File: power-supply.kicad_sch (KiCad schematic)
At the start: 107 parts, among them IC1 TPS54561QDPR, J10 Molex_Pico-Lock_1x02_504050-0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, J5 Molex_Pico-Lock_1x02_504050-0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, Q1 BSS138PW, Q2 BSS138PW, Q3 BSS138PW, Q4 BSS138PW, Q5 BSS138PW, Q6 BSS138PW, U10 TPS62823DLCT, U11 TPS62823DLCT, U12 TPS62823DLCT, U13 TPS62823DLCT, U16 TPS62823DLCT, U9 LM3881MME_NOPB

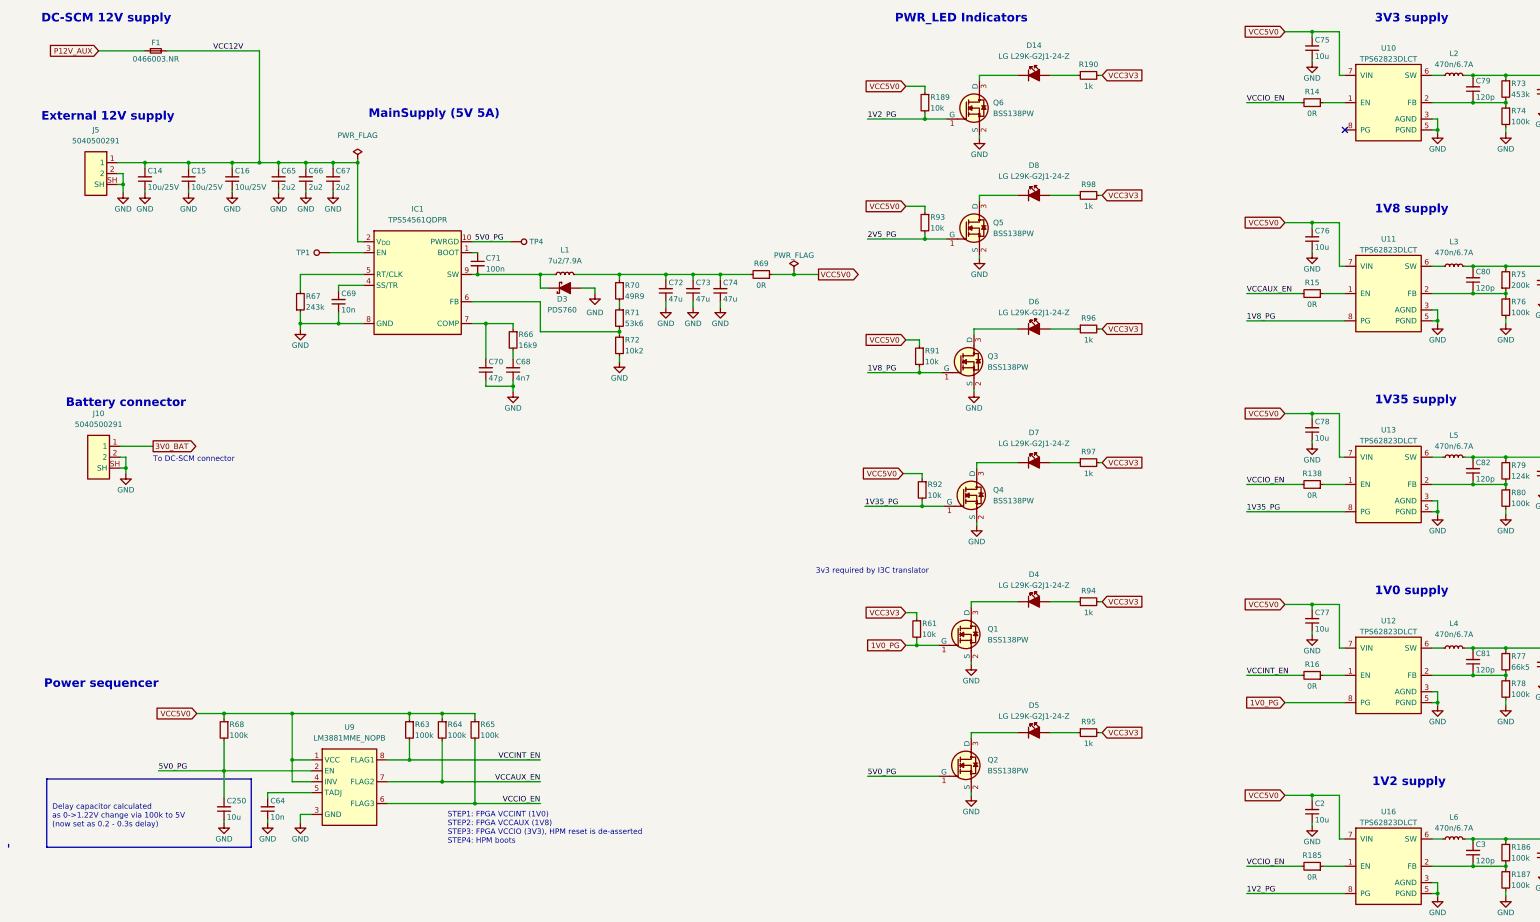
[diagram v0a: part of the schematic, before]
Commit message: [#55652] Fix hotareas
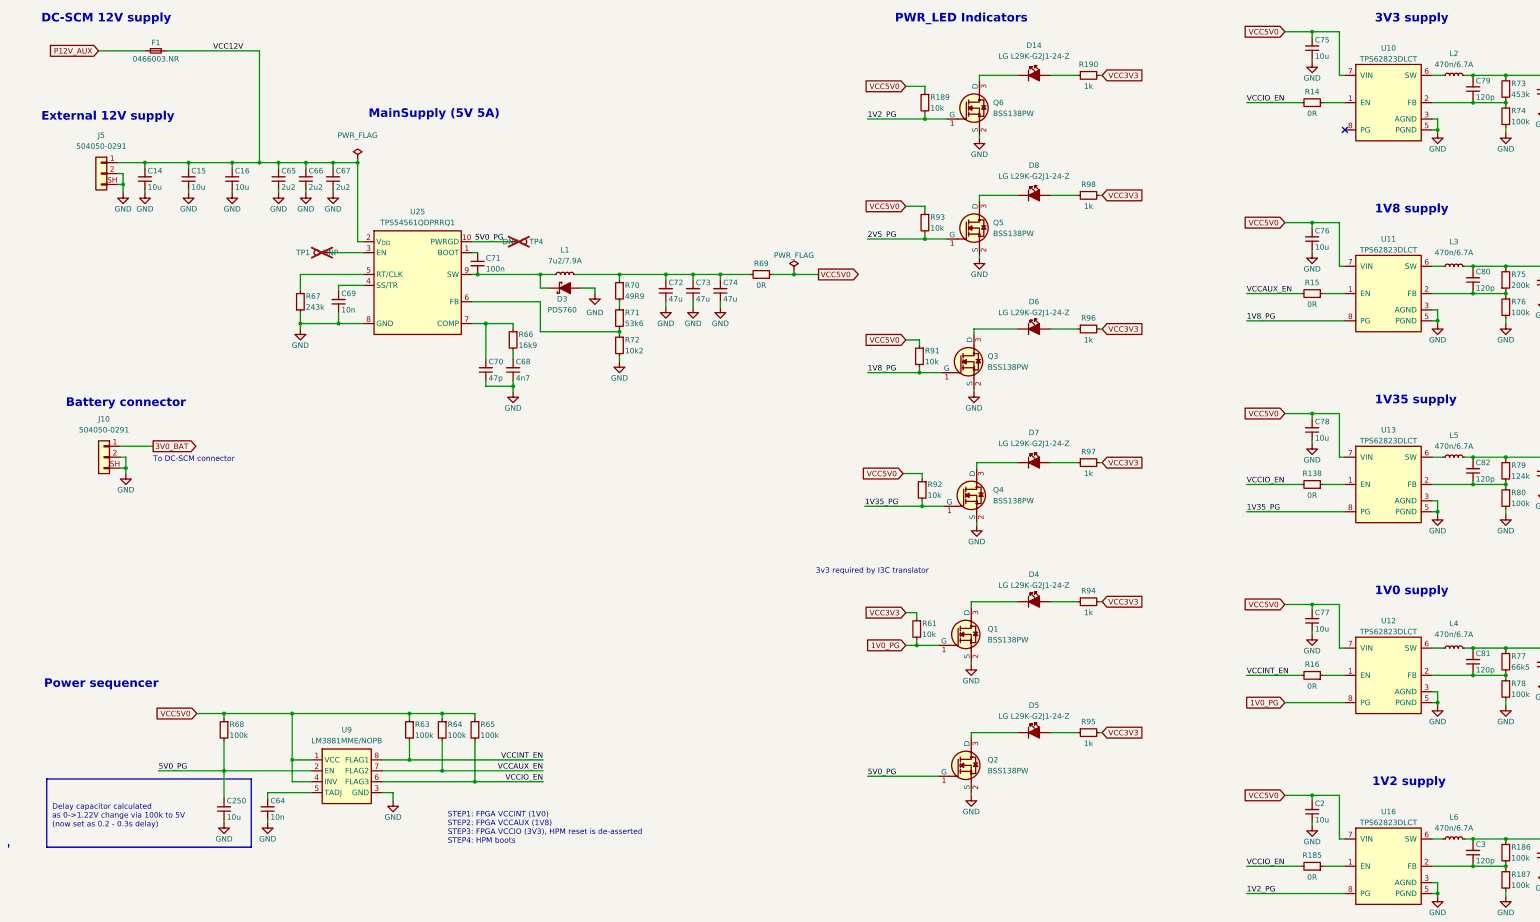
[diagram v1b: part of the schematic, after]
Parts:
- C101, C103, C250, C83, C84, C85, C86, C87, C88, C89, C90: Manufacturer Yaego -> YAGEO
- C14, C15, C16: Val 10u/25V -> 10u; Voltage (none) -> 25V
- C70: MPN GRM1555C1E470JA01D -> C0402C470J5GACTU; Manufacturer Murata -> KEMET
- D14, D4, D5, D6, D7, D8: Manufacturer Osram -> OSRAM
- F1: value 0466003.NR -> F_3A_1206
- J10, J5: value Molex_Pico-Lock_1x02_504050-0291 -> Molex_Pico-Lock_1x2_504050-0291; footprint antmicro-footprints:Molex_Pico-Lock_504050-0291_1x02_1MP_P1.5mm -> antmicro-footprints:Conn_Molex_Pico-Lock_1x2_504050-0291; symbol antmicroRectangularConnectorsHeadersMalePins:Molex_Pico-Lock_1x02_504050-0291 -> antmicroWire2BoardConnectors:Molex_Pico-Lock_1x2_504050-0291; MPN 5040500291 -> 504050-0291
- L1: value 7447798720 -> L_7u2_7.9A_WE-PDF-1064; footprint antmicro-footprints:L_WE-PDF -> antmicro-footprints:L_WE-PDF-1064; symbol antmicroFixedInductors:L_7u2_7.9A_WE-PDF -> antmicroFixedInductors:L_7u2_7.9A_WE-PDF-1064; IMax (none) -> 7.9 A; ISat (none) -> 6 A
- L2, L3, L4, L5, L6: value IHLP1212AEERR47M11 -> L_470n_6.7A_Vishay-IHLP-1212AE-11; footprint antmicro-footprints:L_Vishay_IHLP-1212 -> antmicro-footprints:L_Vishay-IHLP-1212AE; symbol antmicroFixedInductors:IHLP1212AEERR47M11 -> antmicroFixedInductors:L_470n_6.7A_Vishay-IHLP-1212AE-11; IMax (none) -> 6.7 A; ISat (none) -> 6.7 A
- R69: Manufacturer Multicomp -> Multicomp Pro
- TP1, TP4: value TP_SMD1MM -> TP_1mm_SMD; footprint antmicro-footprints:Testpoint_smd_1mm -> antmicro-footprints:TP_SMD_1mm; now not fitted; now left out of the parts list
- U10, U11, U12, U13, U16: footprint antmicro-footprints:QFN-8_2x1mm -> antmicro-footprints:QFN-8_2x1.5mm
- U25: renamed from IC1; value TPS54561QDPR -> TPS54561QDPRRQ1; footprint antmicro-footprints:WSON-10_4x4 -> antmicro-footprints:WSON-10-1EP_4x4mm_P0.8mm_EP2.6x3mm
- U9: value LM3881MME_NOPB -> LM3881; symbol antmicroPMICPowerSequencers:LM3881MME_NOPB -> antmicroPMICPowerSequencers:LM3881
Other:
- moved on the sheet: U9

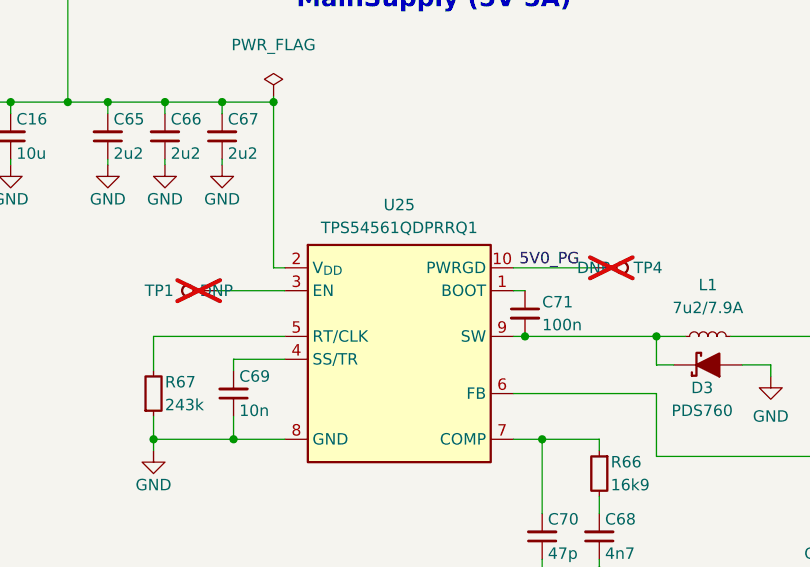
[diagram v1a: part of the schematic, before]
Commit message: [#68236] Update components description
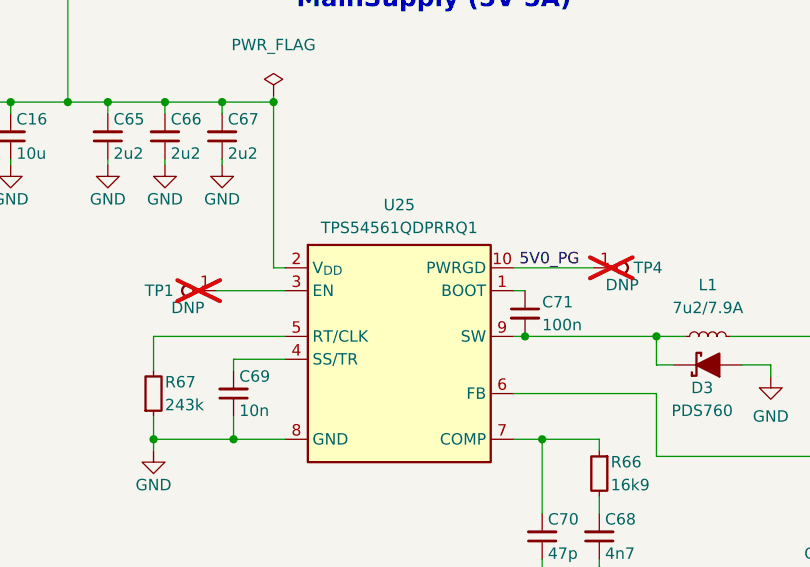
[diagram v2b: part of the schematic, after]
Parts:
- C3, C79, C80, C81, C82: symbol antmicroCapacitors0402:C_120p_0402 -> antmicroCapacitors0402:C_120p_100V_0402

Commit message: [#68236] Allign sch to grid
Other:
- moved on the sheet: C103, C14, C15, C16, C2, C250, C3, C64, C69, C71, C72, C73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

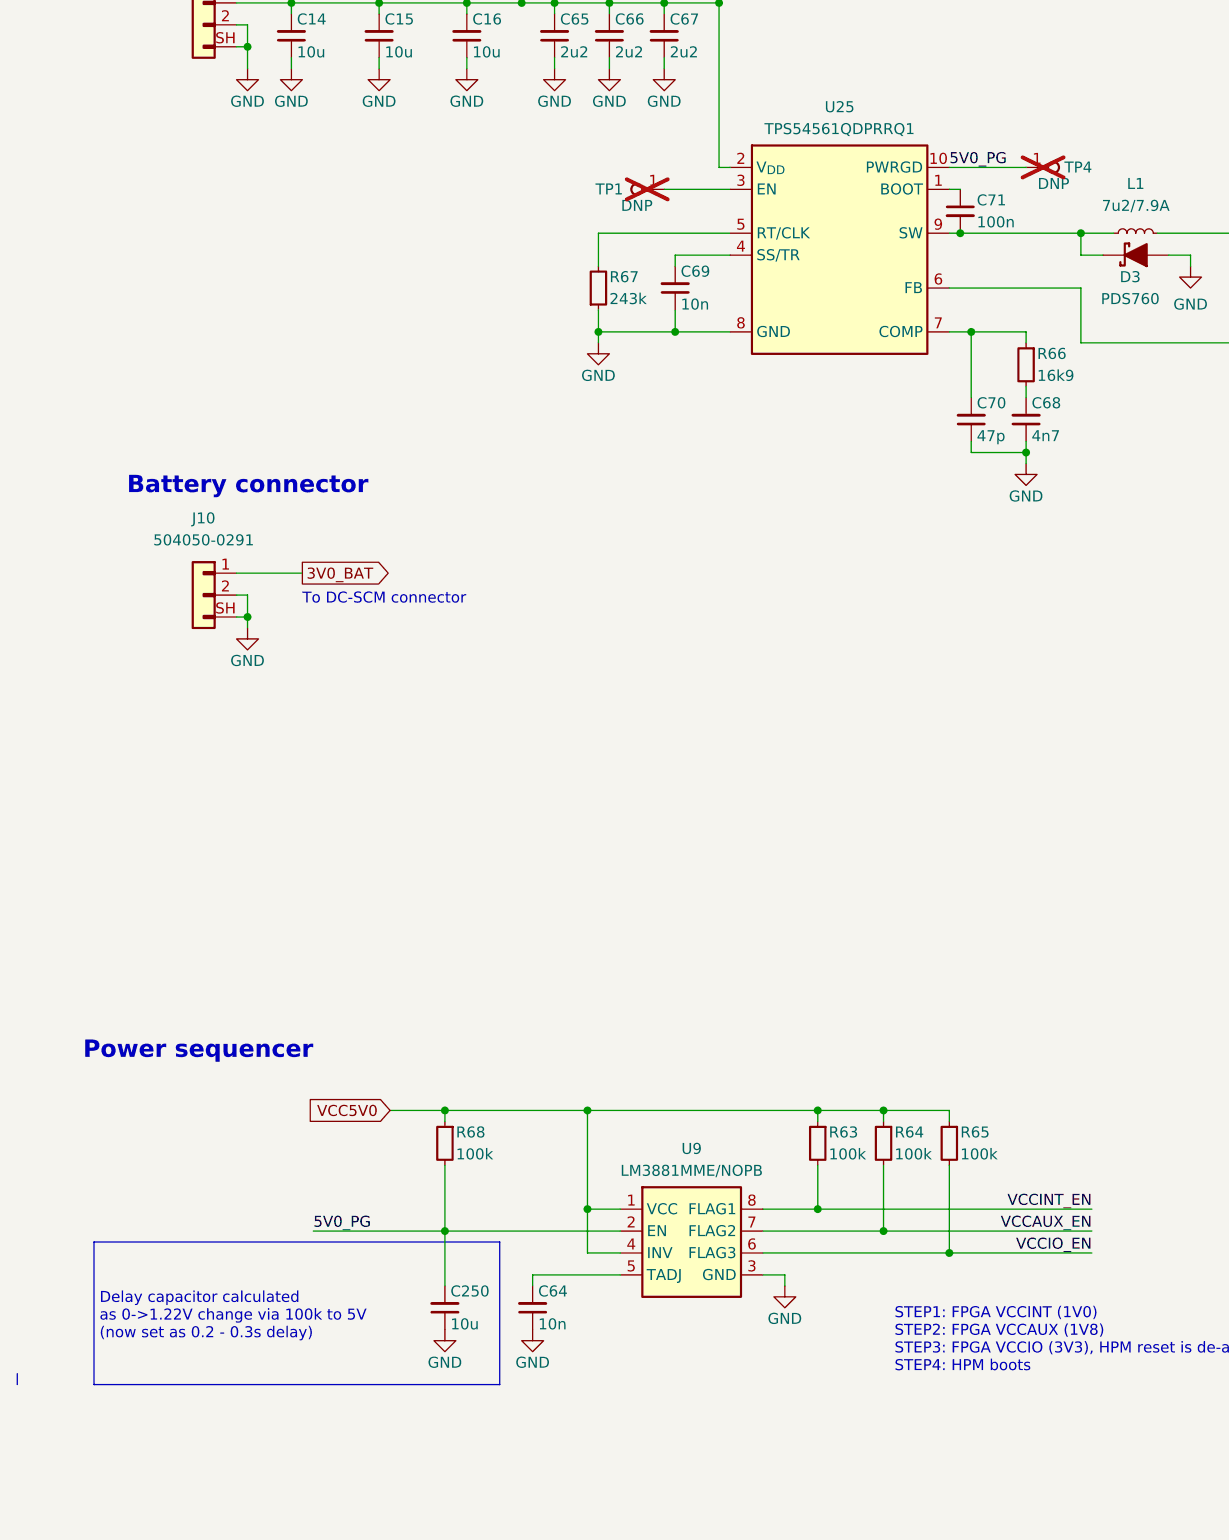
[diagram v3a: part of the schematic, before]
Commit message: [#68236] Remove DNP property from Testpoints
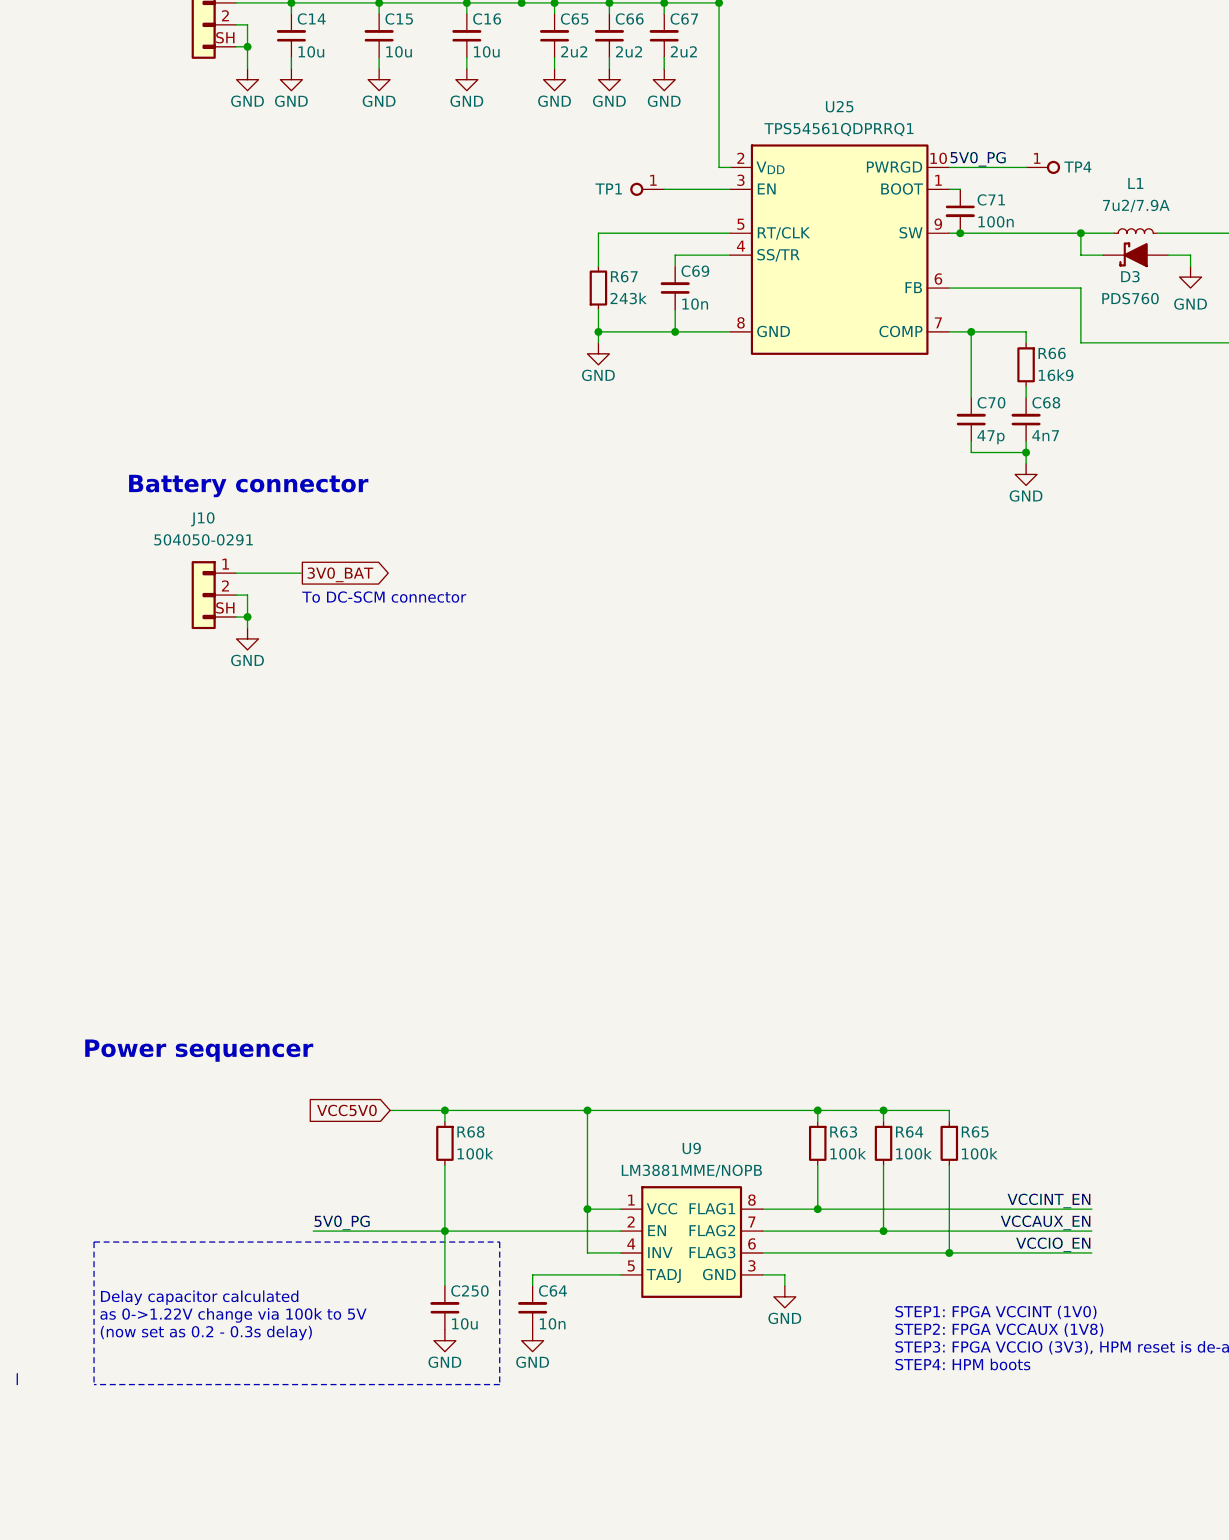
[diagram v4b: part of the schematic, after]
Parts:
- TP1, TP4: DNP DNP -> (none); now fitted
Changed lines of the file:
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@@
   )
   (polyline (pts (xy 68.58 198.12) (xy 68.58 214.63))
-    (stroke (width 0) (type default))
+    (stroke (width 0) (type dash))
   )
   (wire (pts (xy 322.58 212.09) (xy 322.58 201.93))
@@
   )
   (polyline (pts (xy 68.58 214.63) (xy 21.59 214.63))
-    (stroke (width 0) (type default))
+    (stroke (width 0) (type dash))
   )
   (wire (pts (xy 220.98 167.64) (xy 223.52 167.64))
@@
   )
   (polyline (pts (xy 21.59 198.12) (xy 21.59 214.63))
-    (stroke (width 0) (type default))
+    (stroke (width 0) (type dash))
   )
   (wire (pts (xy 388.62 167.64) (xy 393.7 167.64))
@@
   )
   (polyline (pts (xy 21.59 198.12) (xy 68.58 198.12))
-    (stroke (width 0) (type default))
+    (stroke (width 0) (type dash))
   )
   (wire (pts (xy 223.52 167.64) (xy 228.6 167.64))
@@
   )
   (symbol (lib_id "antmicroTestPoints:TP_1mm_SMD") (at 129.54 73.66 0) (unit 1)
-    (in_bom no) (on_board yes) (dnp yes)
+    (in_bom no) (on_board yes) (dnp no)
     (property "Reference" "TP4" (at 133.985 73.66 0)
       (effects (font (size 1.27 1.27)) (justify left))
@@
       (effects (font (size 1.27 1.27) (thickness 0.15)) (justify left bottom) hide)
     )
-    (property "DNP" "DNP" (at 132.715 75.565 0)
-      (effects (font (size 1.27 1.27)))
-    )
     (pin "1")
     (instances
@@
   )
   (symbol (lib_id "antmicroTestPoints:TP_1mm_SMD") (at 87.63 76.2 180) (unit 1)
-    (in_bom no) (on_board yes) (dnp yes)
+    (in_bom no) (on_board yes) (dnp no)
     (property "Reference" "TP1" (at 81.28 76.2 0)
       (effects (font (size 1.27 1.27)))
@@
       (effects (font (size 1.27 1.27) (thickness 0.15)) (justify left bottom) hide)
     )
-    (property "DNP" "DNP" (at 84.455 78.105 0)
-      (effects (font (size 1.27 1.27)))
-    )
     (pin "1")
